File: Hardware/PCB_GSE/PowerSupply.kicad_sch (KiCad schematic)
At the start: 69 parts, among them J2 Vin_XT30PW-F, U3 MPQ9843GLE-5-AEC1-Z, U4 TLV75733PDBVR

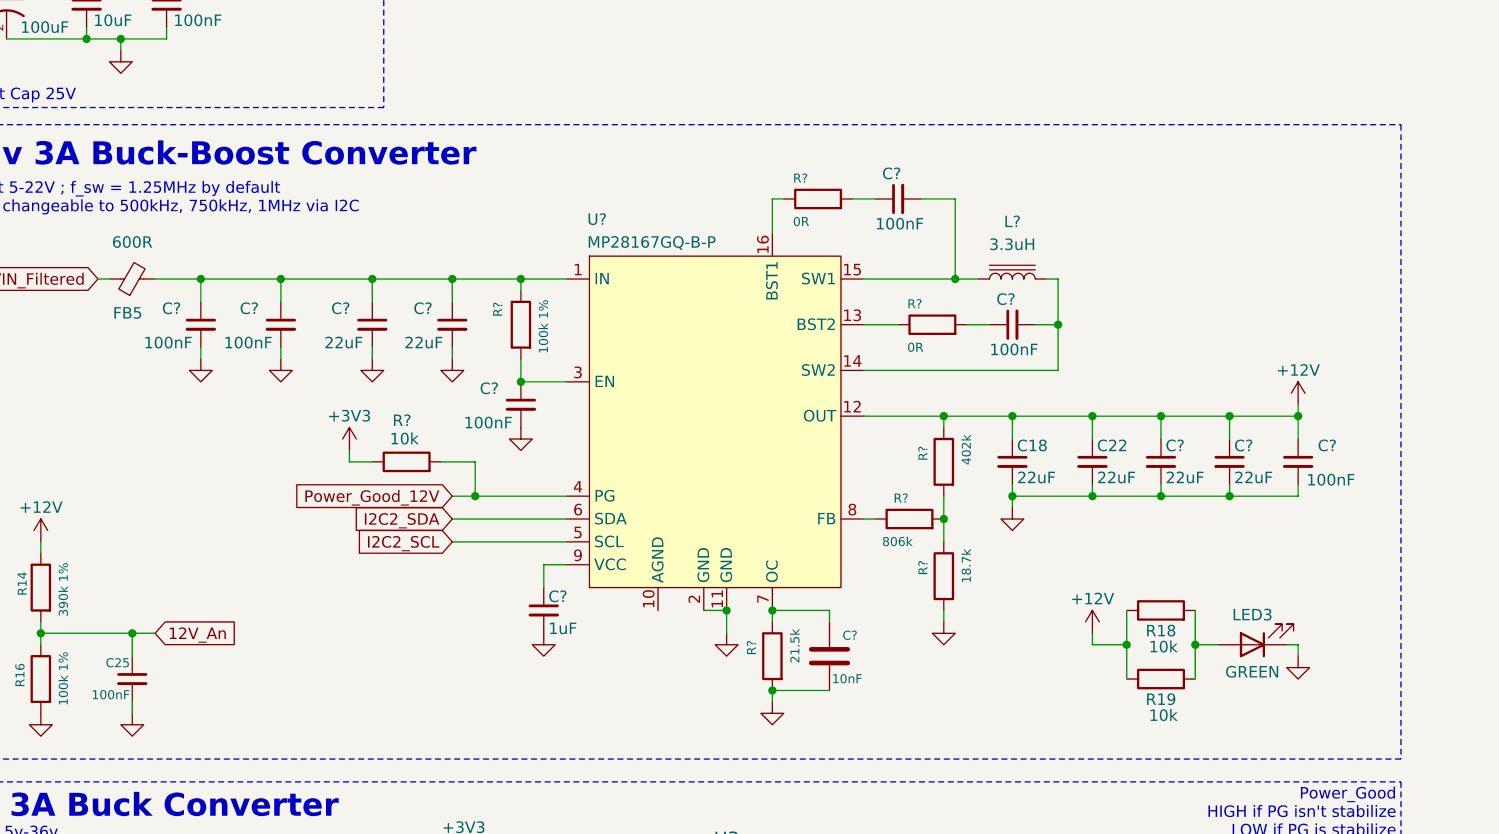
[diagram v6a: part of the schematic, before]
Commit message: wip : add BOM for 12V buck-boost
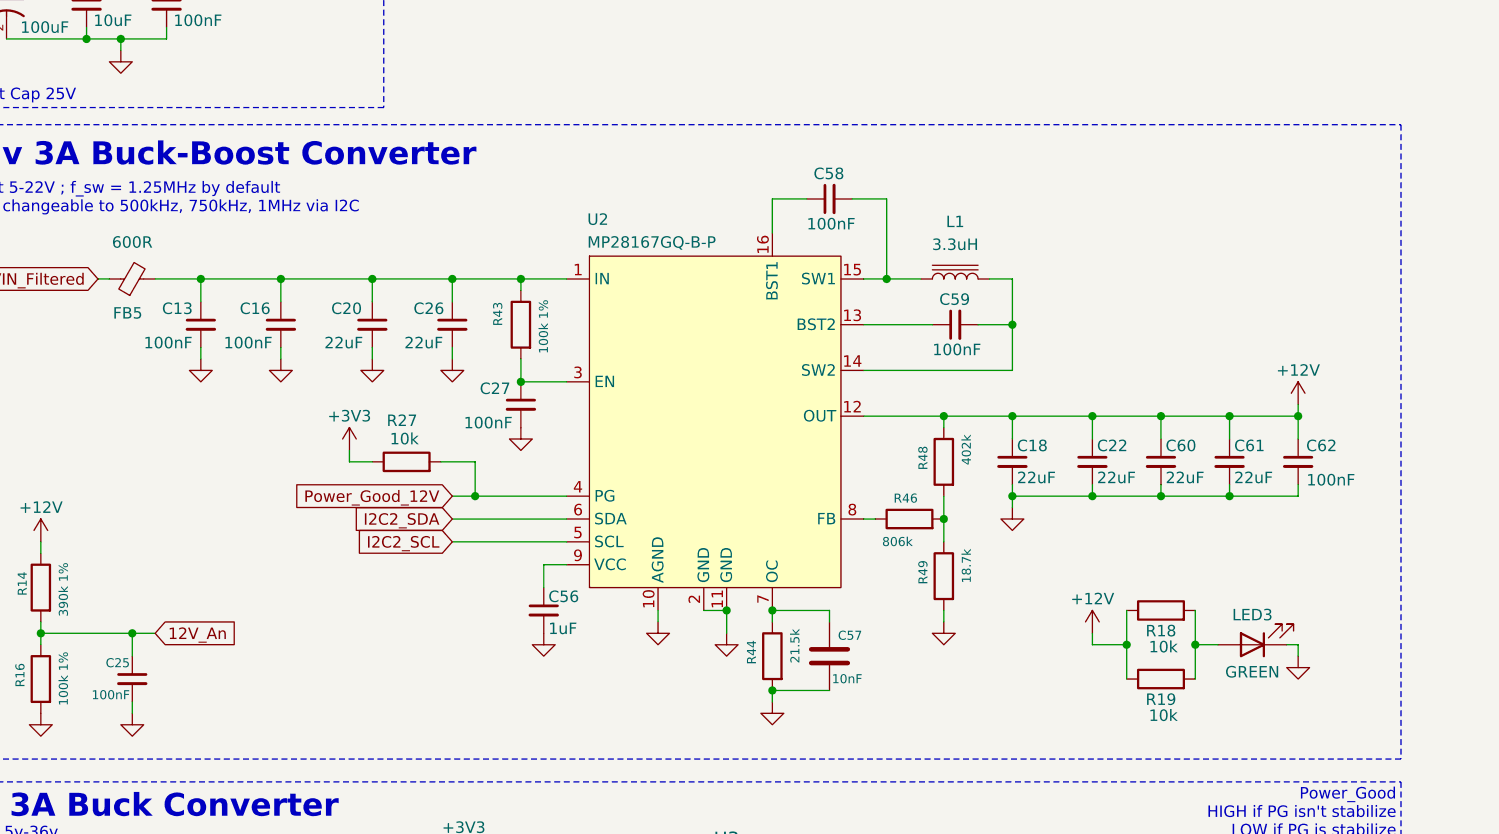
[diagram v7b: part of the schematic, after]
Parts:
- removed R? (x2): 0R, Resistor_SMD:R_0805_2012Metric, symbol Device:R
- R44: renamed from R?; DigiKey_Part_Number (none) -> 541-21.5KCCT-ND; Manufacturer_Part_Number (none) -> CRCW080521K5FKEA
- R46: renamed from R?; DigiKey_Part_Number (none) -> 311-806KCRCT-ND; Manufacturer_Part_Number (none) -> RC0805FR-07806KL
- R48: renamed from R?; DigiKey_Part_Number (none) -> 311-402KCRCT-ND; Manufacturer_Part_Number (none) -> RC0805FR-07402KL
- R49: renamed from R?; DigiKey_Part_Number (none) -> RMCF0805FT18K7CT-ND; Manufacturer_Part_Number (none) -> RMCF0805FT18K7
- U2: renamed from U?; DigiKey_Part_Number (none) -> 1589-MP28167GQ-B-PCT-ND; Manufacturer_Part_Number (none) -> MP28167GQ-B-P
- gave numbers to parts that had none: 15
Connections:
- net AGND5V: now also U2.10 (AGND)
- net at U2.16 (BST1): now also C58.1
- net at U2.13 (BST2): now also C59.1
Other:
- moved on the sheet: C58, C59, L1

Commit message: wip : subsystems layout
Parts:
- renumbered C10 to C12, C11 to C13, C25 to C14, C12 to C15, C14 to C16, C13 to C17, C15 to C18, C17 to C19, C16 to C20, C19 to C21, C21 to C22, C20 to C23, C23 to C24, C26 to C25, C24 to C26, C56 to C28, C58 to C29, C57 to C30, C59 to C31, C28 to C32, C29 to C33, C30 to C34, C18 to C35, C31 to C36, C22 to C37, C60 to C38, C61 to C39, C62 to C40, C32 to C41, C33 to C42, C35 to C43, C34 to C44, FB5 to FB2, R16 to R15, R27 to R16, R12 to R17, R13 to R18, R43 to R19, R15 to R20, R44 to R21, R17 to R22, R46 to R23, R48 to R24, R49 to R25, R20 to R26, R18 to R27, R19 to R28, R22 to R29, R11 to R30, R21 to R31, R26 to R32, R23 to R33, R24 to R34, R25 to R35, U3 to U2, U2 to U3
